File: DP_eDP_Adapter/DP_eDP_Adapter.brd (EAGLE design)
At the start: 50 x 50 mm, 37 parts, among them IC1 TLC5947XLP

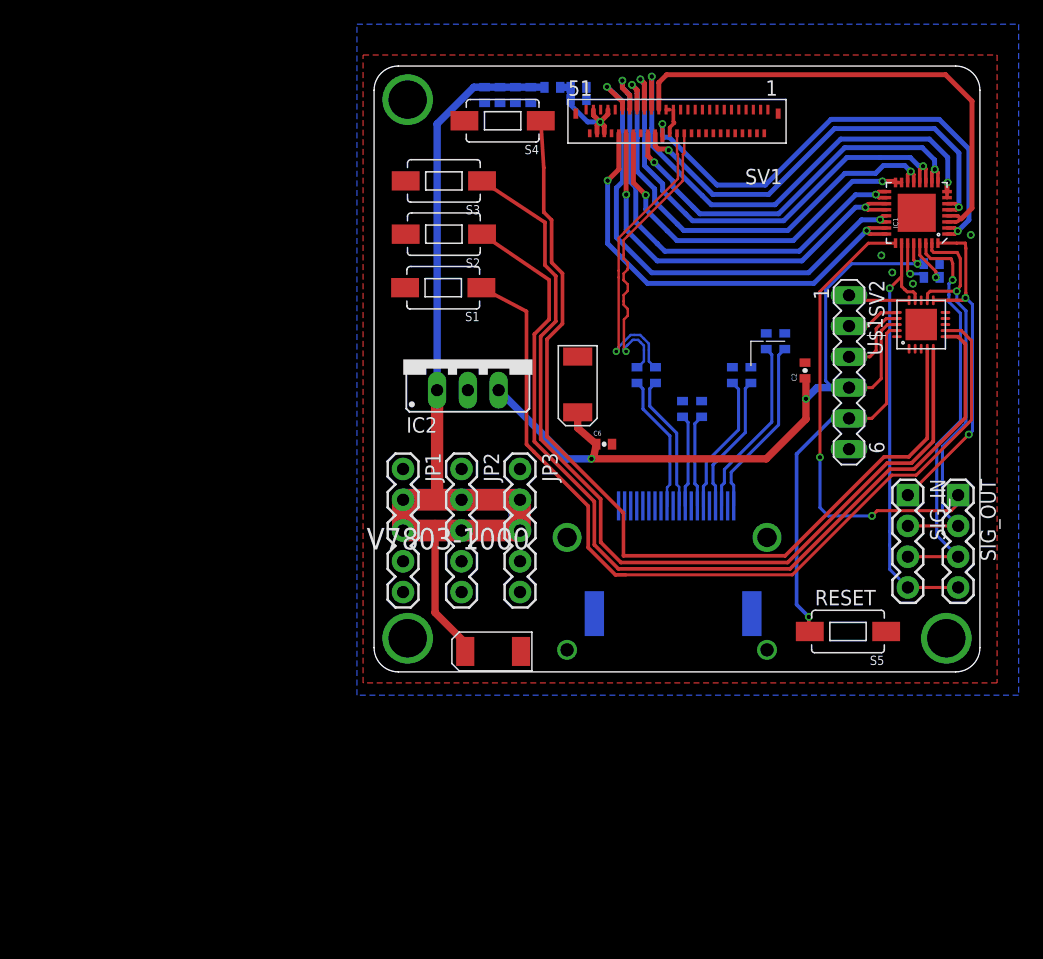
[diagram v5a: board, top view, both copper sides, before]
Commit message: 
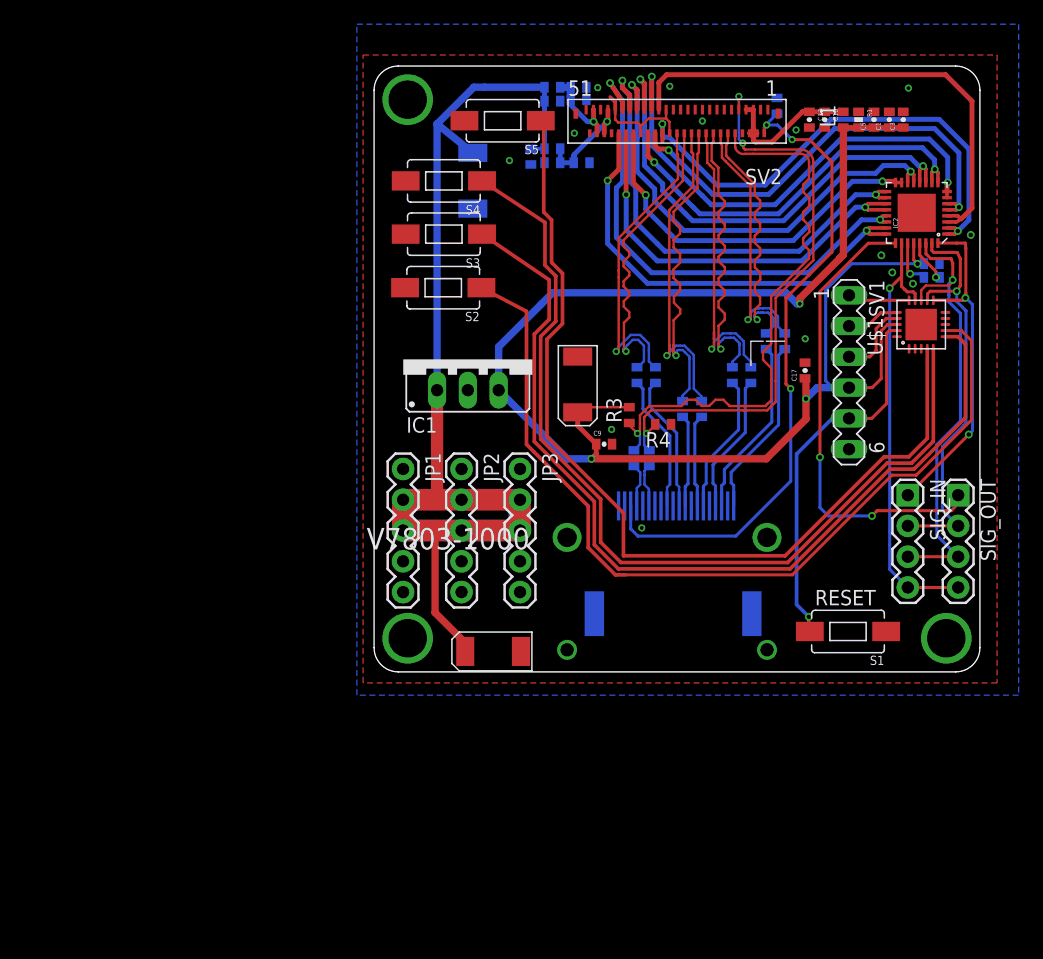
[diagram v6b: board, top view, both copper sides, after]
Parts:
- added C19, C20, C21, C22, C23, C24, C25, C26, C27: (no value), DP_eDP_Adapter:SPARKFUN-PASSIVES_0402-CAP
- added L2, L3: 240ohm-300ma, rcl:R0402
- added R3, R4, R5: 100K, rcl:R0402
- C1: value 0.1uF -> .1uf; device SparkFun:0402-CAP -> SparkFun-Passives:0402-CAP
- C10: value (none) -> 82pF; device DP_eDP_Adapter:SPARKFUN-PASSIVES_0402-CAP -> SparkFun-Passives:0402-CAP
- C11, C12: value (none) -> 100pF 50V; device DP_eDP_Adapter:SPARKFUN-PASSIVES_0402-CAP -> SparkFun-Passives:0402-CAP
- C13: value (none) -> 1000pF; device DP_eDP_Adapter:SPARKFUN-PASSIVES_0402-CAP -> SparkFun-Passives:0402-CAP
- C14, C6: value .1uf -> 820pF 50V
- C15: value 0.1uF -> 820pF 50V
- C16, C17: value 82pF -> 0.1uF; device SparkFun-Passives:0402-CAP -> SparkFun:0402-CAP
- C18: value 1000pF -> (none); device SparkFun-Passives:0402-CAP -> DP_eDP_Adapter:SPARKFUN-PASSIVES_0402-CAP
- C2: value 0.1uF -> 10uF 50V; device SparkFun:0402-CAP -> SparkFun-Passives:EIA6032
- C3: value (none) -> 0.1uF; device DP_eDP_Adapter:SPARKFUN-PASSIVES_0402-CAP -> SparkFun-Passives:0402-CAP
- C4: value 10uF -> 100uF 50V
- C5: value 10uF -> 82pF; device SparkFun-Passives:EIA6032 -> SparkFun-Passives:0402-CAP
- C7: value (none) -> 820pF 50V; device DP_eDP_Adapter:SPARKFUN-PASSIVES_0402-CAP -> SparkFun-Passives:0402-CAP
- C8: value (none) -> 10uF; device DP_eDP_Adapter:SPARKFUN-PASSIVES_0402-CAP -> SparkFun-Passives:EIA6032
- C9: value (none) -> .1uf; device DP_eDP_Adapter:SPARKFUN-PASSIVES_0402-CAP -> SparkFun-Passives:0402-CAP
- IC1: value TLC5947XLP -> (none); device slice_noshift:QFN32_XLP -> v-reg:78XXS
- IC2: value (none) -> TLC5947XLP; device v-reg:78XXS -> slice_noshift:QFN32_XLP
- L1: value (none) -> 240ohm-300ma
- SV1: value EDP_CONNECTOR -> (none); device DP_eDP_Adapter:EDP_MOLEX -> NSL:MA06-1
- SV2: value (none) -> EDP_CONNECTOR; device NSL:MA06-1 -> DP_eDP_Adapter:EDP_MOLEX
- moved S5 50.9 mm to (-14.4, 20.5)
- moved S1 43.8 mm to (14.1, -21.7)
- moved IC1 39.0 mm to (-17.3, 0.79), turned to 0 degrees
- moved IC2 39.0 mm to (19.8, 12.9), turned to 90 degrees
- moved C4 38.9 mm to (-16.9, 15.5), flipped to the bottom, turned to 270 degrees
- moved C16 35.9 mm to (21.0, 8.69), turned to 180 degrees
- moved C2 34.6 mm to (-15.2, -23.3), turned to 0 degrees
- moved C5 32.8 mm to (16.3, 20.6)
- moved C17 29.9 mm to (10.6, -0.13), flipped to the top, turned to 90 degrees
- moved C6 28.6 mm to (-10.3, 22.1), flipped to the bottom, turned to 180 degrees
- moved R1 28.4 mm to (15.0, 20.6), flipped to the top, turned to 270 degrees
- moved C11 27.9 mm to (-8.13, 23.2), turned to 180 degrees
- moved C10 25.9 mm to (12.2, 20.6), flipped to the top, turned to 270 degrees
- moved C13 25.4 mm to (10.9, 20.6), flipped to the top, turned to 270 degrees
- moved C18 25.3 mm to (7.37, 2.29), turned to 90 degrees
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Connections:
- removed net LED_POS: C17.1, C18.1, L1.2, SV1.P$45, SV1.P$46, SV1.P$48, SV1.P$49
- removed net N$12: SV1.P$9
- removed net N$14: SV1.P$10
- removed net N$7: SV1.P$2
- new net AUX_CH_N: C26.1, R3.1, SV2.P$10
- new net AUX_CH_P: C27.1, R4.2, SV2.P$9
- new net AUX_N: C26.2, U$2.P$17
- new net AUX_P: C27.2, U$2.P$15
- new net HPD: R5.2, SV2.P$2, U$2.P$18
- new net LED_POS_1: C11.1, C14.1, L2.2, SV2.P$48, SV2.P$49
- new net LED_POS_2: C12.1, C15.1, L3.2, SV2.P$45, SV2.P$46
- net +3V3: now also C16.1, C17.1, C3.1, C5.1, C8.P$1, C9.1, IC1.OUT, IC2.28, L1.1, R1.2, R3.2, SV1.4; no longer C2.1, C5.P$1, C6.1, IC1.28, IC2.OUT, SV2.4
- net 20V: now also C2.P$1, C6.1, C7.1, IC1.IN, L2.1, L3.1; no longer C14.1, C15.1, C16.1, IC2.IN, L1.1, R1.2
- net BLANK: now also IC2.30; no longer IC1.30
- net BUTTON_1: now also S2.P$1; no longer S1.P$1
- net BUTTON_2: now also S3.P$1; no longer S2.P$1
- net BUTTON_3: now also S4.P$1; no longer S3.P$1
- net BUTTON_4: now also S5.P$1; no longer S4.P$1
- net GND: now also C10.2, C11.2, C12.2, C13.2, C2.P$2, C3.2, C5.2, C7.2, C8.P$2, C9.2, IC1.GND, IC2.29, R4.1, R5.1, S1.P$1, S5.P$2, SV1.6, SV2.P$1, SV2.P$11, SV2.P$15, SV2.P$19, SV2.P$23, SV2.P$27, SV2.P$28, SV2.P$29, SV2.P$3, SV2.P$36, SV2.P$43, SV2.P$51, SV2.P$8; no longer C18.2, C2.2, C5.P$2, IC1.29, IC2.GND, S1.P$2, S5.P$1, SV1.P$1, SV1.P$11, SV1.P$15, SV1.P$19, SV1.P$23, SV1.P$27, SV1.P$28, SV1.P$29, SV1.P$3, SV1.P$36, SV1.P$43, SV1.P$51, SV1.P$8, SV2.6
- net LANE0_N: now also C18.2, SV2.P$12; no longer C7.2, SV1.P$12
- net LANE0_P: now also C22.2, SV2.P$14; no longer C3.2, SV1.P$14
- net LANE1_N: now also C19.2, SV2.P$16; no longer C9.2, SV1.P$16
- net LANE1_P: now also C23.2, SV2.P$18; no longer C8.2, SV1.P$18
- net LANE2_N: now also C20.2, SV2.P$20; no longer C11.2, SV1.P$20
- net LANE2_P: now also C24.2, SV2.P$22; no longer C10.2, SV1.P$22
- net LANE3_N: now also C21.2, SV2.P$24; no longer C13.2, SV1.P$24
- net LANE3_P: now also C25.2, SV2.P$26; no longer C12.2, SV1.P$26
- net LED_NEG_1A: now also IC2.23, IC2.24, SV2.P$42; no longer IC1.23, IC1.24, SV1.P$42
- net LED_NEG_1B: now also IC2.11, IC2.12, SV2.P$35; no longer IC1.11, IC1.12, SV1.P$35
- net LED_NEG_2A: now also IC2.21, IC2.22, SV2.P$41; no longer IC1.21, IC1.22, SV1.P$41
- net LED_NEG_2B: now also IC2.10, IC2.9, SV2.P$34; no longer IC1.10, IC1.9, SV1.P$34
- net LED_NEG_3A: now also IC2.19, IC2.20, SV2.P$40; no longer IC1.19, IC1.20, SV1.P$40
- net LED_NEG_3B: now also IC2.7, IC2.8, SV2.P$33; no longer IC1.7, IC1.8, SV1.P$33
- net LED_NEG_4A: now also IC2.17, IC2.18, SV2.P$39; no longer IC1.17, IC1.18, SV1.P$39
- net LED_NEG_4B: now also IC2.5, IC2.6, SV2.P$32; no longer IC1.5, IC1.6, SV1.P$32
- net LED_NEG_5A: now also IC2.15, IC2.16, SV2.P$38; no longer IC1.15, IC1.16, SV1.P$38
- net LED_NEG_5B: now also IC2.3, IC2.4, SV2.P$31; no longer IC1.3, IC1.4, SV1.P$31
- net LED_NEG_6A: now also IC2.13, IC2.14, SV2.P$37; no longer IC1.13, IC1.14, SV1.P$37
- net LED_NEG_6B: now also IC2.1, IC2.2, SV2.P$30; no longer IC1.1, IC1.2, SV1.P$30
- net MISO: now also SV1.2; no longer SV2.2
- net MOSI: now also SV1.1; no longer SV2.1
- net N$13: now also IC2.27; no longer IC1.27
- net N$15_N: now also C19.1; no longer C9.1
- net N$15_P: now also C23.1; no longer C8.1
- net N$17_N: now also C20.1; no longer C11.1
- net N$17_P: now also C24.1; no longer C10.1
- net N$19_N: now also C21.1; no longer C13.1
- net N$19_P: now also C25.1; no longer C12.1
- net N$3_N: now also C18.1; no longer C7.1
- net N$3_P: now also C22.1; no longer C3.1
- net RST: now also S1.P$2, SV1.5; no longer S5.P$2, SV2.5
- net SCK: now also SV1.3; no longer SV2.3
- net SCLK: now also IC2.31; no longer IC1.31
- net SIN: now also IC2.32; no longer IC1.32
- net SOUT: now also IC2.25; no longer IC1.25
- net VIN: now also C10.1, C13.1, L1.2, SV2.P$4, SV2.P$5, SV2.P$6, SV2.P$7; no longer SV1.P$4, SV1.P$5, SV1.P$6, SV1.P$7
- net XLAT: now also IC2.26; no longer IC1.26
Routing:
- net +3V3: track 69.9 -> 126.5 mm, vias 3 -> 4
- net HPD: track 0.00 -> 54.3 mm, vias 0 -> 3
- net AUX_CH_P: track 0.00 -> 49.1 mm, vias 0 -> 3
- net AUX_CH_N: track 0.00 -> 47.4 mm, vias 0 -> 1
- net LANE2_N: track 0.00 -> 28.0 mm, vias 0 -> 1
- net LANE2_P: track 0.00 -> 27.5 mm, vias 0 -> 1
- net LANE1_N: track 0.00 -> 26.2 mm, vias 0 -> 1
- net LANE1_P: track 0.00 -> 25.1 mm, vias 0 -> 1
- net LANE0_N: track 0.00 -> 22.3 mm, vias 0 -> 1
- net LANE0_P: track 0.00 -> 21.4 mm, vias 0 -> 1
- net VIN: track 0.00 -> 12.3 mm
- net 20V: track 105.0 -> 115.0 mm
- net LED_POS: track 9.98 -> 0.00 mm, vias 1 -> 0
- net LED_POS_2: track 0.00 -> 8.89 mm, vias 0 -> 1
- net GND: track 5.83 -> 12.8 mm, vias 5 -> 15
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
